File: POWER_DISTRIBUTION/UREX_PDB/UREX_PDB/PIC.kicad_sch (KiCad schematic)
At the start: 19 parts, among them IC4 INA232AIDDFR

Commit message: LAYOUT FINISHED, DRC NEXT
LESO
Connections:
- net GND: now also PS1.4 (NC)
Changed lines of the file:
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@@
 	(wire
 		(pts
+			(xy 135.89 152.4) (xy 138.43 152.4)
+		)
+		(stroke
+			(width 0)
+			(type default)
+		)
+	)
+	(wire
+		(pts
 			(xy 44.45 62.23) (xy 36.83 62.23)
 		)
@@
 	(wire
 		(pts
+			(xy 138.43 149.86) (xy 138.43 152.4)
+		)
+		(stroke
+			(width 0)
+			(type default)
+		)
+	)
+	(wire
+		(pts
 			(xy 152.4 154.94) (xy 175.26 154.94)
 		)
@@
 					(unit 1)
 				)
+			)
+		)
+	)
+	(symbol
+		(lib_id "power:GND")
+		(at 138.43 149.86 180)
+		(unit 1)
+		(body_style 1)
+		(exclude_from_sim no)
+		(in_bom yes)
+		(on_board yes)
+		(in_pos_files yes)
+		(dnp no)
+		(fields_autoplaced yes)
+		(property "Reference" "#PWR041"
+			(at 138.43 143.51 0)
+			(hide yes)
+			(show_name no)
+			(do_not_autoplace no)
+			(effects
+				(font
+					(size 1.27 1.27)
+				)
+			)
+		)
+		(property "Value" "GND"
+			(at 138.43 144.78 0)
+			(show_name no)
+			(do_not_autoplace no)
+			(effects
+				(font
+					(size 1.27 1.27)
+				)
+			)
+		)
+		(property "Footprint" ""
+			(at 138.43 149.86 0)
+			(hide yes)
+			(show_name no)
+			(do_not_autoplace no)
+			(effects
+				(font
+					(size 1.27 1.27)
+				)
+			)
+		)
+		(property "Datasheet" ""
+			(at 138.43 149.86 0)
+			(hide yes)
+			(show_name no)
+			(do_not_autoplace no)
+			(effects
+				(font
+					(size 1.27 1.27)
+				)
+			)
+		)
+		(property "Description" "Power symbol creates a global label with name \"GND\" , ground"
+			(at 138.43 149.86 0)
+			(hide yes)
+			(show_name no)
+			(do_not_autoplace no)
+			(effects
+				(font
+					(size 1.27 1.27)
+				)
+			)
+		)
+		(pin "1"
+		)
+		(instances
+			(project "UREX_PDB"
+				(path "/a38818e8-e869-45a4-b642-866064a1ec6a/b3eb405f-da3d-4f70-ac2c-72d781132e9f"
+					(reference "#PWR041")
+					(unit 1)
+				)

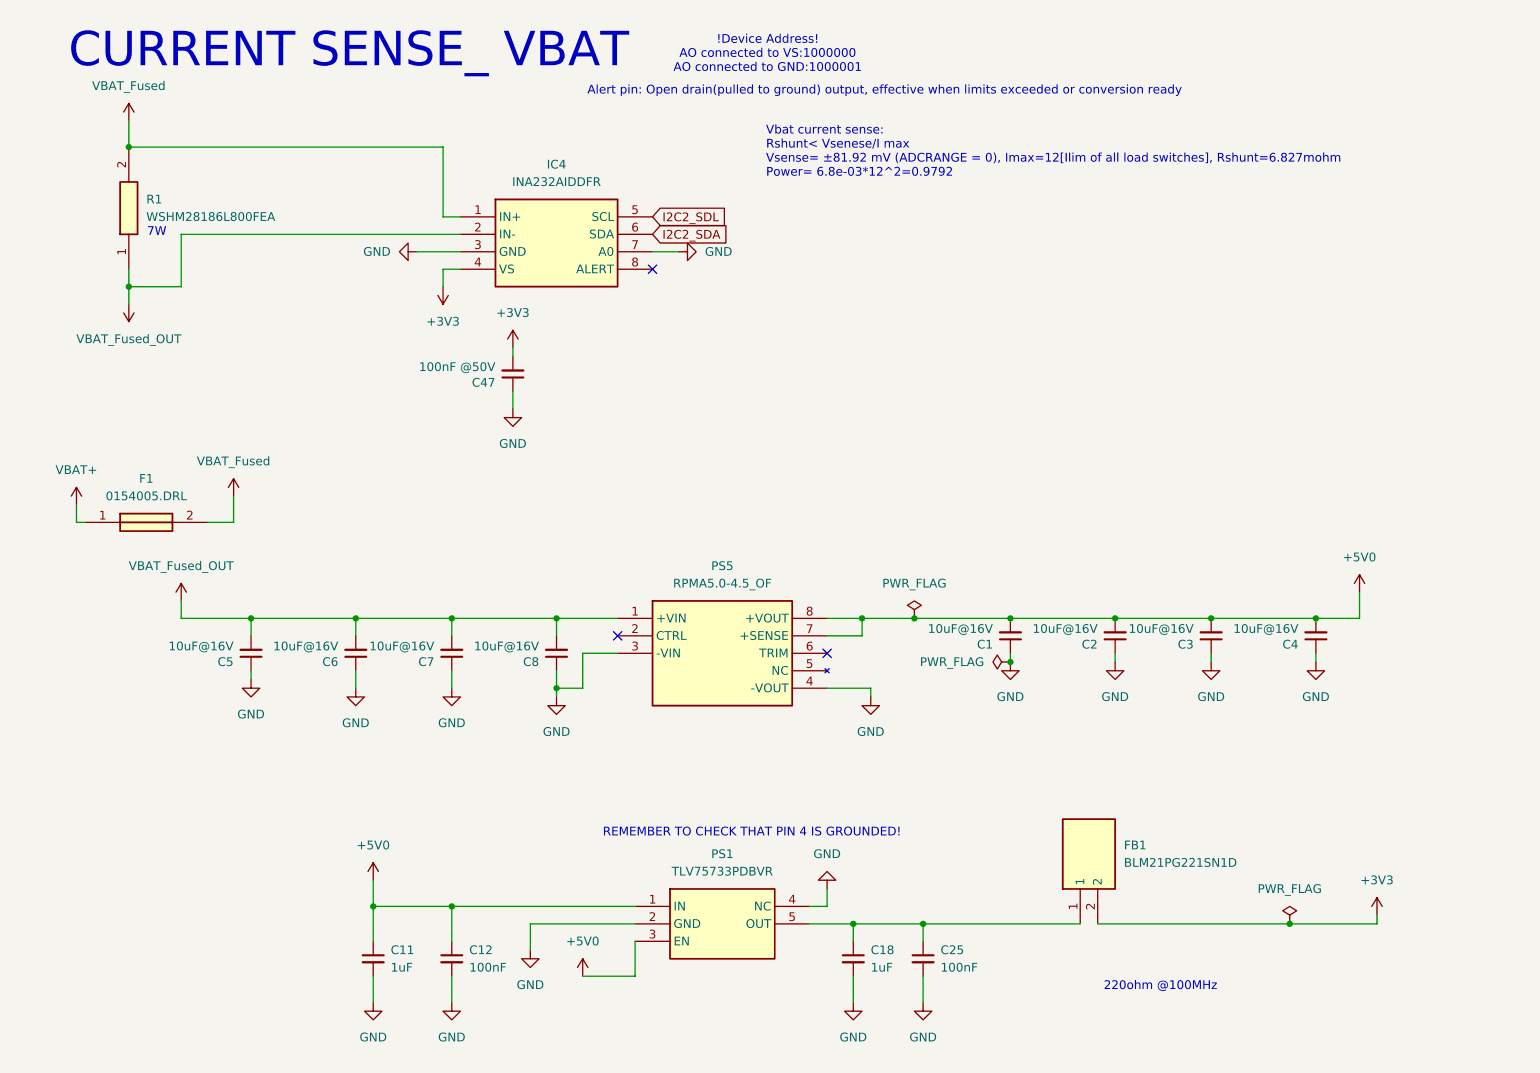
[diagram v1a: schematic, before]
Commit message: added 5v 8A  dcdc
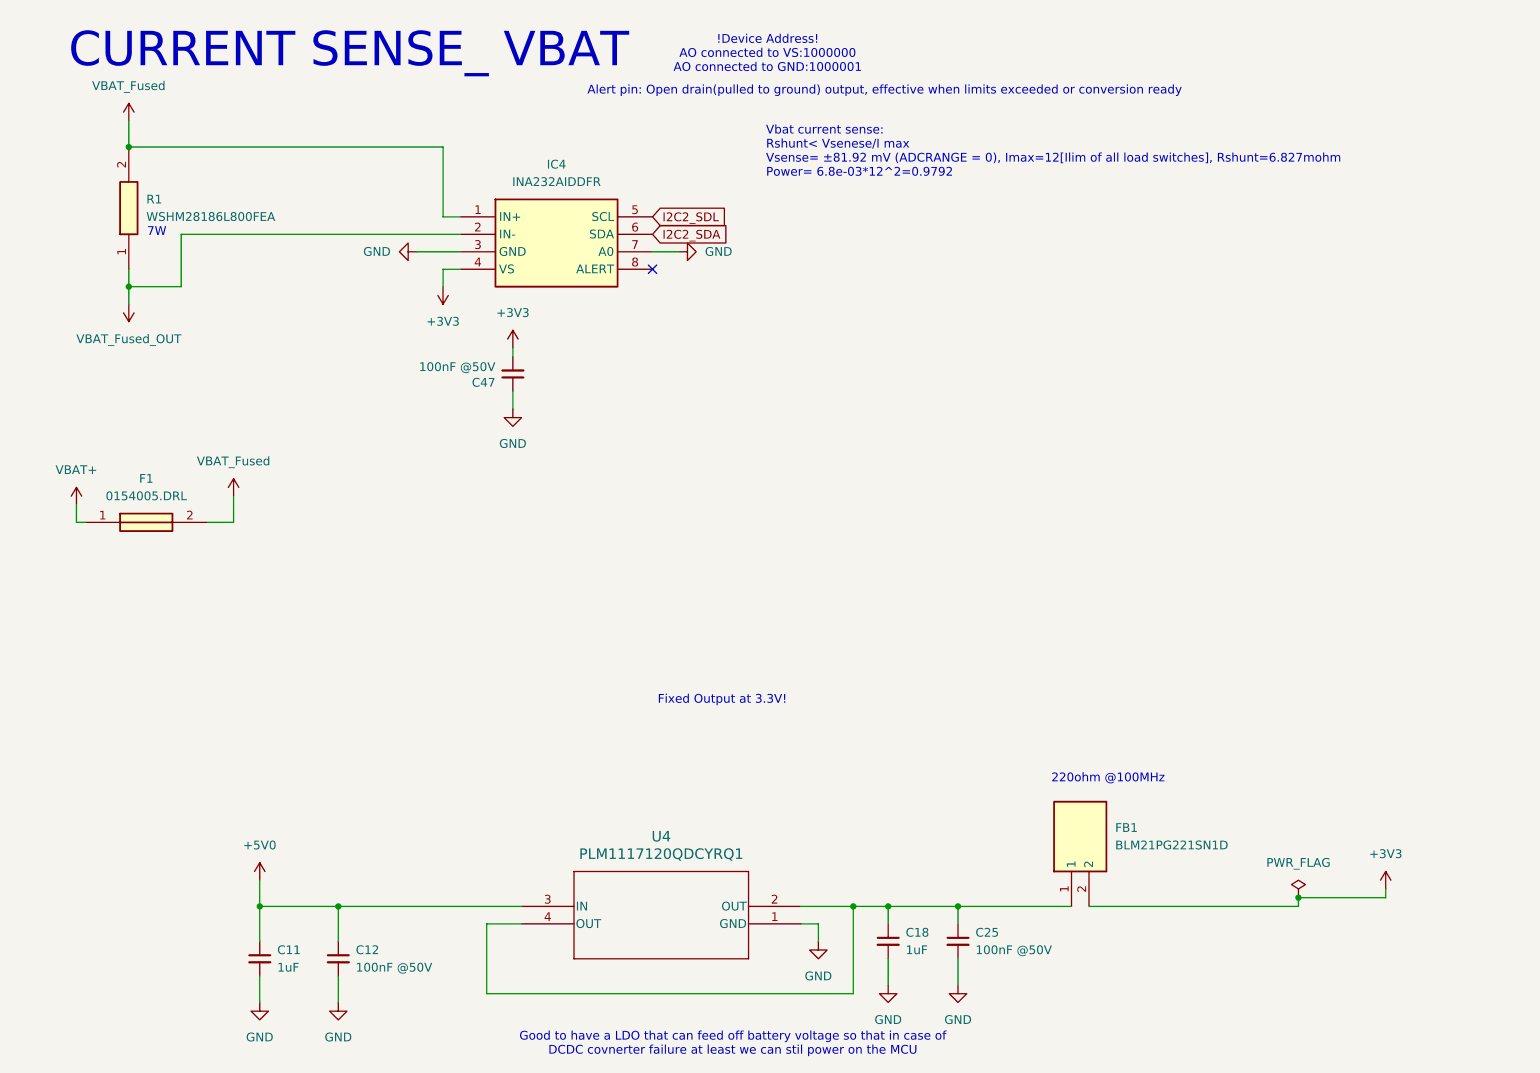
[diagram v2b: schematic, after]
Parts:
- removed C1, C2, C3, C4, C5, C6, C7, C8: 10uF@16V, Capacitor_SMD:C_0805_2012Metric_Pad1.18x1.45mm_HandSolder, symbol Device:C_Small
- removed PS1: TLV75733PDBVR, SamacSys_Parts:SOT95P280X145-5N, symbol SamacSys_Parts:TLV75733PDBVR
- removed PS5: RPMA5.0-4.5_OF, SamacSys_Parts:RPMA5045OF, symbol SamacSys_Parts:RPMA5.0-4.5_OF
- added U4: PLM1117120QDCYRQ1, LM1117120QDCYRQ1:SOT-223-4_DCY_TEX, symbol LM1117120QDCYRQ1:PLM1117120QDCYRQ1
- C12, C25: value 100nF -> 100nF @50V
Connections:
- net +5V0: now also U4.3 (IN)
- net GND: now also U4.1 (GND)
- net at C18.1, C25.1, FB1.1: now also U4.2 (OUT), U4.4 (OUT)
- no-connect marks 3 -> 1
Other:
- note added: "Fixed Output at 3.3V!"
- note added: "Good to have a LDO that can feed off battery voltage so that in case of DCDC covnerter failure at least we can stil power on the MCU"
- note removed: "REMEMBER TO CHECK THAT PIN 4 IS GROUNDED!"
- moved on the sheet: C11, C12, C18, C25, FB1

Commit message: V1 Full Fabrication(Freezed design)
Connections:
- net +5V0 is gone; now on net VBAT_Fused_OUT: C11.1, C12.1, U4.3 (IN)
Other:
- note added: "TLV76133DCYR"
